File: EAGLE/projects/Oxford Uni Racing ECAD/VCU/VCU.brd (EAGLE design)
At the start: 165.1 x 114 mm, 3 parts, among them J1 T821108A1S100CEU, X2 D-SUB9-H2M09ST

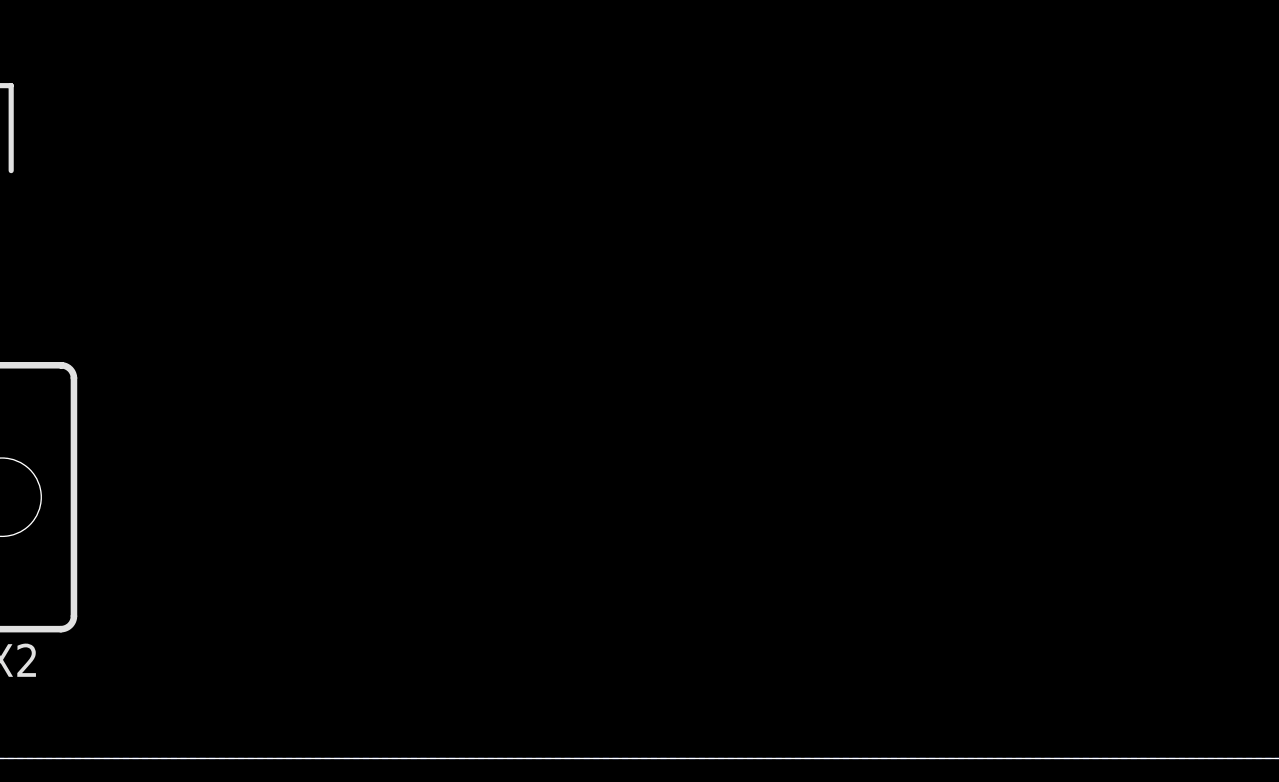
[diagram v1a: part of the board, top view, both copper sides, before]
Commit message: added power delivery to VCU
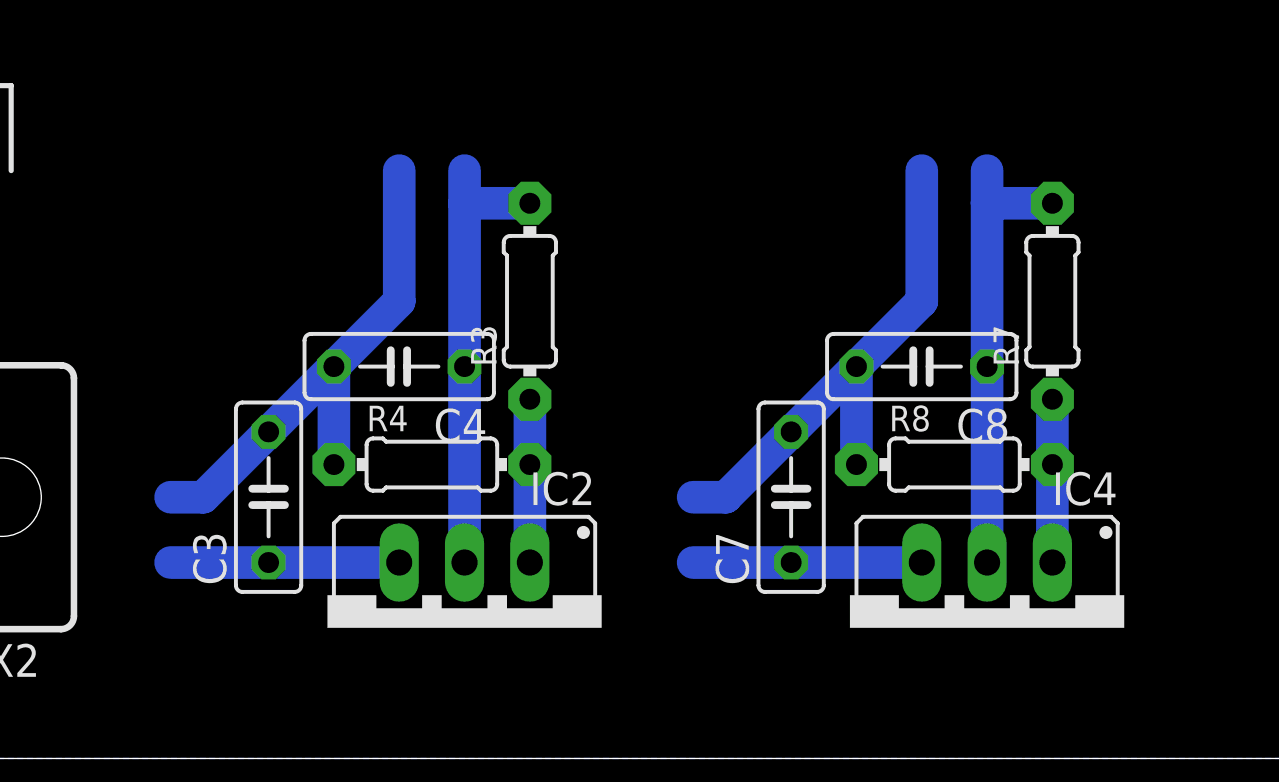
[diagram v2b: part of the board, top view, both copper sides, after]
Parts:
- added C3, C7: 0.1uF, adafruit:C050-025X075
- added C4, C8: 1uF, adafruit:C050-025X075
- added IC2, IC4: (no value), v-reg:317TS
- added R3, R7: 240, adafruit:0204/7
- added R4: 390, adafruit:0204/7
- added R8: 720, adafruit:0204/7
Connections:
- new net 3.3V: C4.1, IC2.2, R3.2
- new net N$2: IC2.1, R3.1, R4.2
- new net N$4: IC4.1, R7.1, R8.2
- net 12V: now also C3.1, C7.1, IC2.3, IC4.3
- net 5V: now also C8.1, IC4.2, R7.2
- net GND: now also C3.2, C4.2, C7.2, C8.2, R4.1, R8.1
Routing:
- net GND: track 31.0 -> 72.8 mm
- net 5V: track 0.00 -> 17.8 mm
- net 3.3V: track 0.00 -> 17.8 mm
- net 12V: track 2.54 -> 20.3 mm
- net N$4: track 0.00 -> 6.35 mm
- net N$2: track 0.00 -> 6.35 mm
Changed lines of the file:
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@@
 <attribute name="VALUE" x="99.06" y="25.4" size="1.27" layer="27" rot="R180" align="center"/>
+</element>
+<element name="IC2" library="v-reg" library_urn="urn:adsk.eagle:library:409" package="317TS" package3d_urn="urn:adsk.eagle:package:30353/1" value="" x="121.92" y="5.08" smashed="yes" rot="R180">
+<attribute name="NAME" x="127" y="11.1252" size="1.27" layer="25" ratio="10" rot="R180"/>
+<attribute name="VALUE" x="127" y="12.7" size="1.27" layer="27" ratio="10" rot="R180"/>
+</element>
+<element name="R3" library="adafruit" library_urn="urn:adsk.eagle:library:420" package="0204/7" package3d_urn="urn:adsk.eagle:package:6240596/1" value="240" x="124.46" y="17.78" smashed="yes" rot="R90">
+<attribute name="NAME" x="123.1646" y="15.24" size="0.9906" layer="25" ratio="12" rot="R90"/>
+<attribute name="VALUE" x="124.9426" y="16.1544" size="0.9906" layer="27" ratio="12" rot="R90"/>
+</element>
+<element name="R4" library="adafruit" library_urn="urn:adsk.eagle:library:420" package="0204/7" package3d_urn="urn:adsk.eagle:package:6240596/1" value="390" x="120.65" y="11.43" smashed="yes">
+<attribute name="NAME" x="118.11" y="12.7254" size="0.9906" layer="25" ratio="12"/>
+<attribute name="VALUE" x="119.0244" y="10.9474" size="0.9906" layer="27" ratio="12"/>
+</element>
+<element name="C3" library="adafruit" library_urn="urn:adsk.eagle:library:420" package="C050-025X075" package3d_urn="urn:adsk.eagle:package:6240357/1" value="0.1uF" x="114.3" y="10.16" smashed="yes" rot="R90">
+<attribute name="NAME" x="112.649" y="6.731" size="1.27" layer="25" ratio="10" rot="R90"/>
+<attribute name="VALUE" x="117.094" y="6.731" size="1.27" layer="27" ratio="10" rot="R90"/>
+</element>
+<element name="C4" library="adafruit" library_urn="urn:adsk.eagle:library:420" package="C050-025X075" package3d_urn="urn:adsk.eagle:package:6240357/1" value="1uF" x="119.38" y="15.24" smashed="yes" rot="R180">
+<attribute name="NAME" x="122.809" y="13.589" size="1.27" layer="25" ratio="10" rot="R180"/>
+<attribute name="VALUE" x="122.809" y="18.034" size="1.27" layer="27" ratio="10" rot="R180"/>
+</element>
+<element name="IC4" library="v-reg" library_urn="urn:adsk.eagle:library:409" package="317TS" package3d_urn="urn:adsk.eagle:package:30353/1" value="" x="142.24" y="5.08" smashed="yes" rot="R180">
+<attribute name="NAME" x="147.32" y="11.1252" size="1.27" layer="25" ratio="10" rot="R180"/>
+<attribute name="VALUE" x="147.32" y="12.7" size="1.27" layer="27" ratio="10" rot="R180"/>
+</element>
+<element name="R7" library="adafruit" library_urn="urn:adsk.eagle:library:420" package="0204/7" package3d_urn="urn:adsk.eagle:package:6240596/1" value="240" x="144.78" y="17.78" smashed="yes" rot="R90">
+<attribute name="NAME" x="143.4846" y="15.24" size="0.9906" layer="25" ratio="12" rot="R90"/>
+<attribute name="VALUE" x="145.2626" y="16.1544" size="0.9906" layer="27" ratio="12" rot="R90"/>
+</element>
+<element name="R8" library="adafruit" library_urn="urn:adsk.eagle:library:420" package="0204/7" package3d_urn="urn:adsk.eagle:package:6240596/1" value="720" x="140.97" y="11.43" smashed="yes">
+<attribute name="NAME" x="138.43" y="12.7254" size="0.9906" layer="25" ratio="12"/>
+<attribute name="VALUE" x="139.3444" y="10.9474" size="0.9906" layer="27" ratio="12"/>
+</element>
+<element name="C7" library="adafruit" library_urn="urn:adsk.eagle:library:420" package="C050-025X075" package3d_urn="urn:adsk.eagle:package:6240357/1" value="0.1uF" x="134.62" y="10.16" smashed="yes" rot="R90">
+<attribute name="NAME" x="132.969" y="6.731" size="1.27" layer="25" ratio="10" rot="R90"/>
+<attribute name="VALUE" x="137.414" y="6.731" size="1.27" layer="27" ratio="10" rot="R90"/>
+</element>
+<element name="C8" library="adafruit" library_urn="urn:adsk.eagle:library:420" package="C050-025X075" package3d_urn="urn:adsk.eagle:package:6240357/1" value="1uF" x="139.7" y="15.24" smashed="yes" rot="R180">
+<attribute name="NAME" x="143.129" y="13.589" size="1.27" layer="25" ratio="10" rot="R180"/>
+<attribute name="VALUE" x="143.129" y="18.034" size="1.27" layer="27" ratio="10" rot="R180"/>
 </element>
 </elements>
@@
 <wire x1="96.52" y1="12.7" x2="96.52" y2="20.32" width="1.27" layer="16"/>
 <wire x1="96.52" y1="20.32" x2="96.52" y2="22.86" width="1.27" layer="16"/>
+<contactref element="C3" pad="2"/>
+<contactref element="R4" pad="1"/>
+<contactref element="C4" pad="2"/>
+<wire x1="114.3" y1="12.7" x2="111.76" y2="10.16" width="1.27" layer="16"/>
+<wire x1="111.76" y1="10.16" x2="110.49" y2="10.16" width="1.27" layer="16"/>
+<wire x1="114.3" y1="12.7" x2="116.84" y2="15.24" width="1.27" layer="16"/>
+<wire x1="116.84" y1="11.43" x2="116.84" y2="15.24" width="1.27" layer="16"/>
+<wire x1="116.84" y1="15.24" x2="119.38" y2="17.78" width="1.27" layer="16"/>
+<wire x1="119.38" y1="17.78" x2="119.38" y2="22.86" width="1.27" layer="16"/>
+<contactref element="C7" pad="2"/>
+<contactref element="R8" pad="1"/>
+<contactref element="C8" pad="2"/>
+<wire x1="134.62" y1="12.7" x2="132.08" y2="10.16" width="1.27" layer="16"/>
+<wire x1="132.08" y1="10.16" x2="130.81" y2="10.16" width="1.27" layer="16"/>
+<wire x1="134.62" y1="12.7" x2="137.16" y2="15.24" width="1.27" layer="16"/>
+<wire x1="137.16" y1="11.43" x2="137.16" y2="15.24" width="1.27" layer="16"/>
+<wire x1="137.16" y1="15.24" x2="139.7" y2="17.78" width="1.27" layer="16"/>
+<wire x1="139.7" y1="17.78" x2="139.7" y2="22.86" width="1.27" layer="16"/>
+<wire x1="119.38" y1="17.78" x2="130.81" y2="10.16" width="0" layer="19" extent="16-16"/>
+<wire x1="100.33" y1="11.43" x2="110.49" y2="10.16" width="0" layer="19" extent="16-16"/>
 </signal>
 <signal name="CANL">
@@
 <signal name="5V">
 <contactref element="X2" pad="9"/>
+<contactref element="IC4" pad="2"/>
+<contactref element="C8" pad="1"/>
+<contactref element="R7" pad="2"/>
+<wire x1="142.24" y1="7.62" x2="142.24" y2="15.24" width="1.27" layer="16"/>
+<wire x1="142.24" y1="15.24" x2="142.24" y2="21.59" width="1.27" layer="16"/>
+<wire x1="142.24" y1="21.59" x2="142.24" y2="22.86" width="1.27" layer="16"/>
+<wire x1="144.78" y1="21.59" x2="142.24" y2="21.59" width="1.27" layer="16"/>
+<wire x1="87.2871" y1="11.5824" x2="142.24" y2="15.24" width="0" layer="19" extent="1-1"/>
 </signal>
 <signal name="12V">
@@
 <contactref element="J1" pad="2"/>
 <wire x1="99.06" y1="20.32" x2="99.06" y2="22.86" width="1.27" layer="16"/>
+<contactref element="IC2" pad="3"/>
+<contactref element="C3" pad="1"/>
+<wire x1="119.38" y1="7.62" x2="114.3" y2="7.62" width="1.27" layer="16"/>
+<wire x1="114.3" y1="7.62" x2="110.49" y2="7.62" width="1.27" layer="16"/>
+<contactref element="IC4" pad="3"/>
+<contactref element="C7" pad="1"/>
+<wire x1="139.7" y1="7.62" x2="134.62" y2="7.62" width="1.27" layer="16"/>
+<wire x1="134.62" y1="7.62" x2="130.81" y2="7.62" width="1.27" layer="16"/>
+<wire x1="119.38" y1="7.62" x2="130.81" y2="7.62" width="0" layer="19" extent="16-16"/>
+<wire x1="99.06" y1="20.32" x2="110.49" y2="7.62" width="0" layer="19" extent="16-16"/>
+</signal>
+<signal name="N$2">
+<contactref element="IC2" pad="1"/>
+<contactref element="R4" pad="2"/>
+<contactref element="R3" pad="1"/>
+<wire x1="124.46" y1="7.62" x2="124.46" y2="11.43" width="1.27" layer="16"/>
+<wire x1="124.46" y1="13.97" x2="124.46" y2="11.43" width="1.27" layer="16"/>
+</signal>
+<signal name="3.3V">
+<contactref element="IC2" pad="2"/>
+<contactref element="C4" pad="1"/>
+<contactref element="R3" pad="2"/>
+<wire x1="121.92" y1="7.62" x2="121.92" y2="15.24" width="1.27" layer="16"/>
+<wire x1="121.92" y1="15.24" x2="121.92" y2="21.59" width="1.27" layer="16"/>
+<wire x1="121.92" y1="21.59" x2="121.92" y2="22.86" width="1.27" layer="16"/>
+<wire x1="124.46" y1="21.59" x2="121.92" y2="21.59" width="1.27" layer="16"/>
+</signal>
+<signal name="N$4">
+<contactref element="IC4" pad="1"/>
+<contactref element="R8" pad="2"/>
+<contactref element="R7" pad="1"/>
+<wire x1="144.78" y1="7.62" x2="144.78" y2="11.43" width="1.27" layer="16"/>
+<wire x1="144.78" y1="13.97" x2="144.78" y2="11.43" width="1.27" layer="16"/>
 </signal>
 </signals>

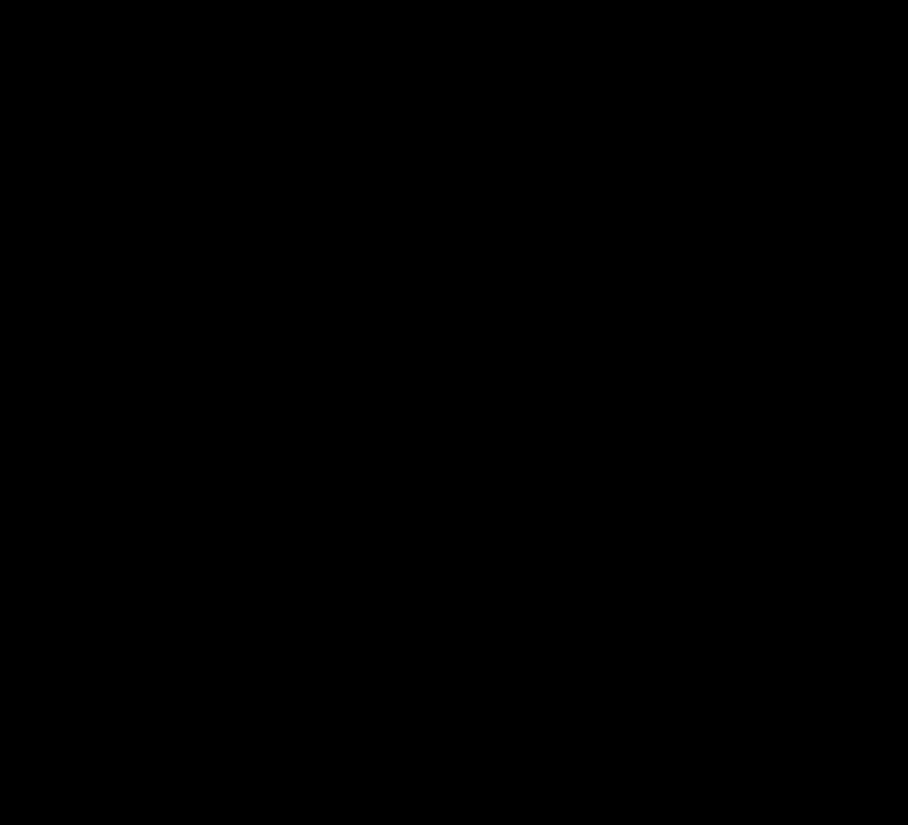
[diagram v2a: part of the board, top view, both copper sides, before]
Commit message: added motor controller output to VCU
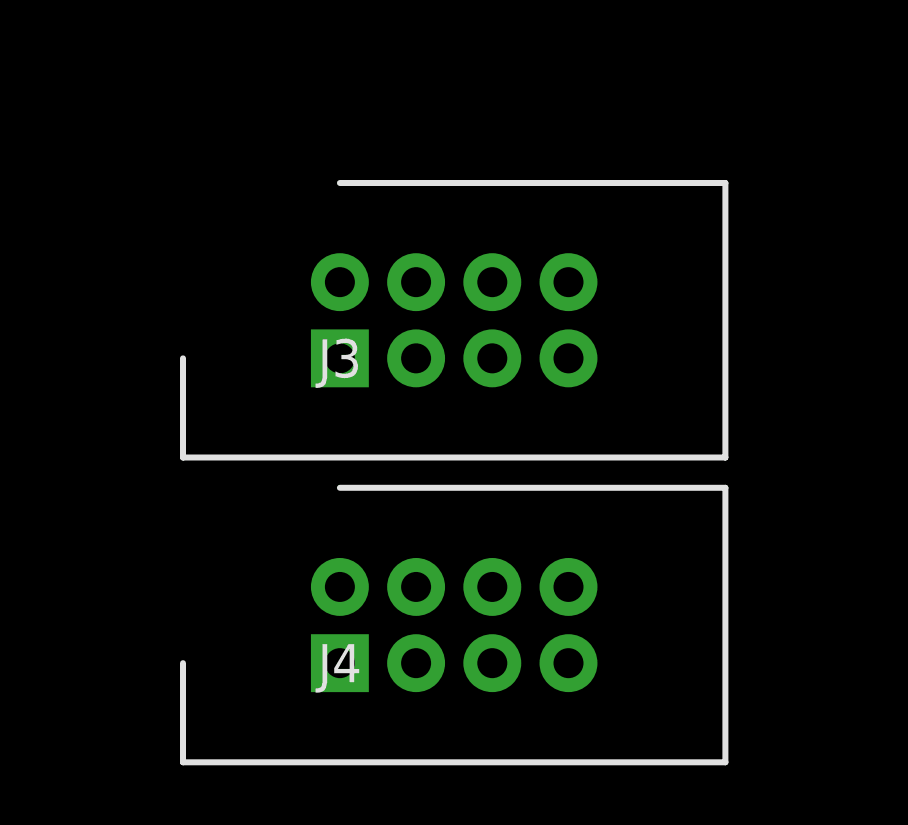
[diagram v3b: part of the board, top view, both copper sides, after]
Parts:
- added J3: MC_LEFT, T821108A1S100CEU:HDRV8W64P254_2X4_1778X895X915P
- added J4: MC_RIGHT, T821108A1S100CEU:HDRV8W64P254_2X4_1778X895X915P
- J1: value T821108A1S100CEU -> PWR_CAN
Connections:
- new net MC_1_BRAKE_INPUT: J3.1
- new net MC_1_IMPULSE_INPUT: J3.4
- new net MC_1_REVERSE_SWITCH: J3.7
- new net MC_1_RXD: J3.3
- new net MC_1_THROTTLE_INPUT: J3.6
- new net MC_1_TXD: J3.5
- new net MC_2_BRAKE_INPUT: J4.1
- new net MC_2_IMPULSE_INPUT: J4.4
- new net MC_2_REVERSE_SWITCH: J4.7
- new net MC_2_RXD: J4.3
- new net MC_2_THROTTLE_INPUT: J4.6
- new net MC_2_TXD: J4.5
- net 5V: now also J3.2, J4.2
- net GND: now also J3.8, J4.8
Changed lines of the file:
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@@
 <attribute name="VALUE" x="91.7956" y="29.6926" size="0.9906" layer="27" ratio="12" rot="R180"/>
 </element>
-<element name="J1" library="T821108A1S100CEU" package="HDRV8W64P254_2X4_1778X895X915P" value="T821108A1S100CEU" x="99.06" y="22.86" smashed="yes" rot="R180">
+<element name="J1" library="T821108A1S100CEU" package="HDRV8W64P254_2X4_1778X895X915P" value="PWR_CAN" x="99.06" y="22.86" smashed="yes" rot="R180">
 <attribute name="DESCRIPTION" value="HEADER, VERTICAL, 2.54MM, 8WAY Amphenol T821 Series, 2.54mm Pitch 8 Way 2 Row Straight PCB Header, Solder Termination, 3A" x="102.87" y="22.86" size="1.778" layer="27" rot="R180" display="off"/>
 <attribute name="HEIGHT" value="9.15mm" x="102.87" y="22.86" size="1.778" layer="27" rot="R180" display="off"/>
@@
 <attribute name="NAME" x="143.129" y="13.589" size="1.27" layer="25" ratio="10" rot="R180"/>
 <attribute name="VALUE" x="143.129" y="18.034" size="1.27" layer="27" ratio="10" rot="R180"/>
+</element>
+<element name="J3" library="T821108A1S100CEU" package="HDRV8W64P254_2X4_1778X895X915P" value="MC_LEFT" x="10.16" y="-16.51" smashed="yes">
+<attribute name="DESCRIPTION" value="HEADER, VERTICAL, 2.54MM, 8WAY Amphenol T821 Series, 2.54mm Pitch 8 Way 2 Row Straight PCB Header, Solder Termination, 3A" x="6.35" y="-16.51" size="1.778" layer="27" display="off"/>
+<attribute name="HEIGHT" value="9.15mm" x="6.35" y="-16.51" size="1.778" layer="27" display="off"/>
+<attribute name="MANUFACTURER_NAME" value="Amphenol" x="6.35" y="-16.51" size="1.778" layer="27" display="off"/>
+<attribute name="MANUFACTURER_PART_NUMBER" value="T821108A1S100CEU" x="6.35" y="-16.51" size="1.778" layer="27" display="off"/>
+<attribute name="NAME" x="10.16" y="-16.51" size="1.27" layer="25" align="center"/>
+<attribute name="RS_PART_NUMBER" value="1702738" x="6.35" y="-16.51" size="1.778" layer="27" display="off"/>
+<attribute name="VALUE" x="10.16" y="-16.51" size="1.27" layer="27" align="center"/>
+</element>
+<element name="J4" library="T821108A1S100CEU" package="HDRV8W64P254_2X4_1778X895X915P" value="MC_RIGHT" x="10.16" y="-26.67" smashed="yes">
+<attribute name="DESCRIPTION" value="HEADER, VERTICAL, 2.54MM, 8WAY Amphenol T821 Series, 2.54mm Pitch 8 Way 2 Row Straight PCB Header, Solder Termination, 3A" x="6.35" y="-26.67" size="1.778" layer="27" display="off"/>
+<attribute name="HEIGHT" value="9.15mm" x="6.35" y="-26.67" size="1.778" layer="27" display="off"/>
+<attribute name="MANUFACTURER_NAME" value="Amphenol" x="6.35" y="-26.67" size="1.778" layer="27" display="off"/>
+<attribute name="MANUFACTURER_PART_NUMBER" value="T821108A1S100CEU" x="6.35" y="-26.67" size="1.778" layer="27" display="off"/>
+<attribute name="NAME" x="10.16" y="-26.67" size="1.27" layer="25" align="center"/>
+<attribute name="RS_PART_NUMBER" value="1702738" x="6.35" y="-26.67" size="1.778" layer="27" display="off"/>
+<attribute name="VALUE" x="10.16" y="-26.67" size="1.27" layer="27" align="center"/>
 </element>
 </elements>
@@
 <wire x1="137.16" y1="15.24" x2="139.7" y2="17.78" width="1.27" layer="16"/>
 <wire x1="139.7" y1="17.78" x2="139.7" y2="22.86" width="1.27" layer="16"/>
+<contactref element="J3" pad="8"/>
+<contactref element="J4" pad="8"/>
 <wire x1="119.38" y1="17.78" x2="130.81" y2="10.16" width="0" layer="19" extent="16-16"/>
 <wire x1="100.33" y1="11.43" x2="110.49" y2="10.16" width="0" layer="19" extent="16-16"/>
+<wire x1="17.78" y1="-13.97" x2="91.44" y2="8.7376" width="0" layer="19" extent="1-1"/>
+<wire x1="17.78" y1="-24.13" x2="17.78" y2="-13.97" width="0" layer="19" extent="1-1"/>
 </signal>
 <signal name="CANL">
@@
 <wire x1="142.24" y1="21.59" x2="142.24" y2="22.86" width="1.27" layer="16"/>
 <wire x1="144.78" y1="21.59" x2="142.24" y2="21.59" width="1.27" layer="16"/>
+<contactref element="J3" pad="2"/>
+<contactref element="J4" pad="2"/>
 <wire x1="87.2871" y1="11.5824" x2="142.24" y2="15.24" width="0" layer="19" extent="1-1"/>
+<wire x1="10.16" y1="-13.97" x2="87.2871" y2="11.5824" width="0" layer="19" extent="1-1"/>
+<wire x1="10.16" y1="-24.13" x2="10.16" y2="-13.97" width="0" layer="19" extent="1-1"/>
 </signal>
 <signal name="12V">
@@
 <wire x1="144.78" y1="13.97" x2="144.78" y2="11.43" width="1.27" layer="16"/>
 </signal>
+<signal name="MC_1_BRAKE_INPUT">
+<contactref element="J3" pad="1"/>
+</signal>
+<signal name="MC_1_REVERSE_SWITCH">
+<contactref element="J3" pad="7"/>
+</signal>
+<signal name="MC_1_IMPULSE_INPUT">
+<contactref element="J3" pad="4"/>
+</signal>
+<signal name="MC_1_THROTTLE_INPUT">
+<contactref element="J3" pad="6"/>
+</signal>
+<signal name="MC_1_RXD">
+<contactref element="J3" pad="3"/>
+</signal>
+<signal name="MC_1_TXD">
+<contactref element="J3" pad="5"/>
+</signal>
+<signal name="MC_2_BRAKE_INPUT">
+<contactref element="J4" pad="1"/>
+</signal>
+<signal name="MC_2_RXD">
+<contactref element="J4" pad="3"/>
+</signal>
+<signal name="MC_2_TXD">
+<contactref element="J4" pad="5"/>
+</signal>
+<signal name="MC_2_REVERSE_SWITCH">
+<contactref element="J4" pad="7"/>
+</signal>
+<signal name="MC_2_IMPULSE_INPUT">
+<contactref element="J4" pad="4"/>
+</signal>
+<signal name="MC_2_THROTTLE_INPUT">
+<contactref element="J4" pad="6"/>
+</signal>
 </signals>
